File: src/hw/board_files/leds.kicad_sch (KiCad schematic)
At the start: 19 parts, among them U1 IS31FL3236A-TQ

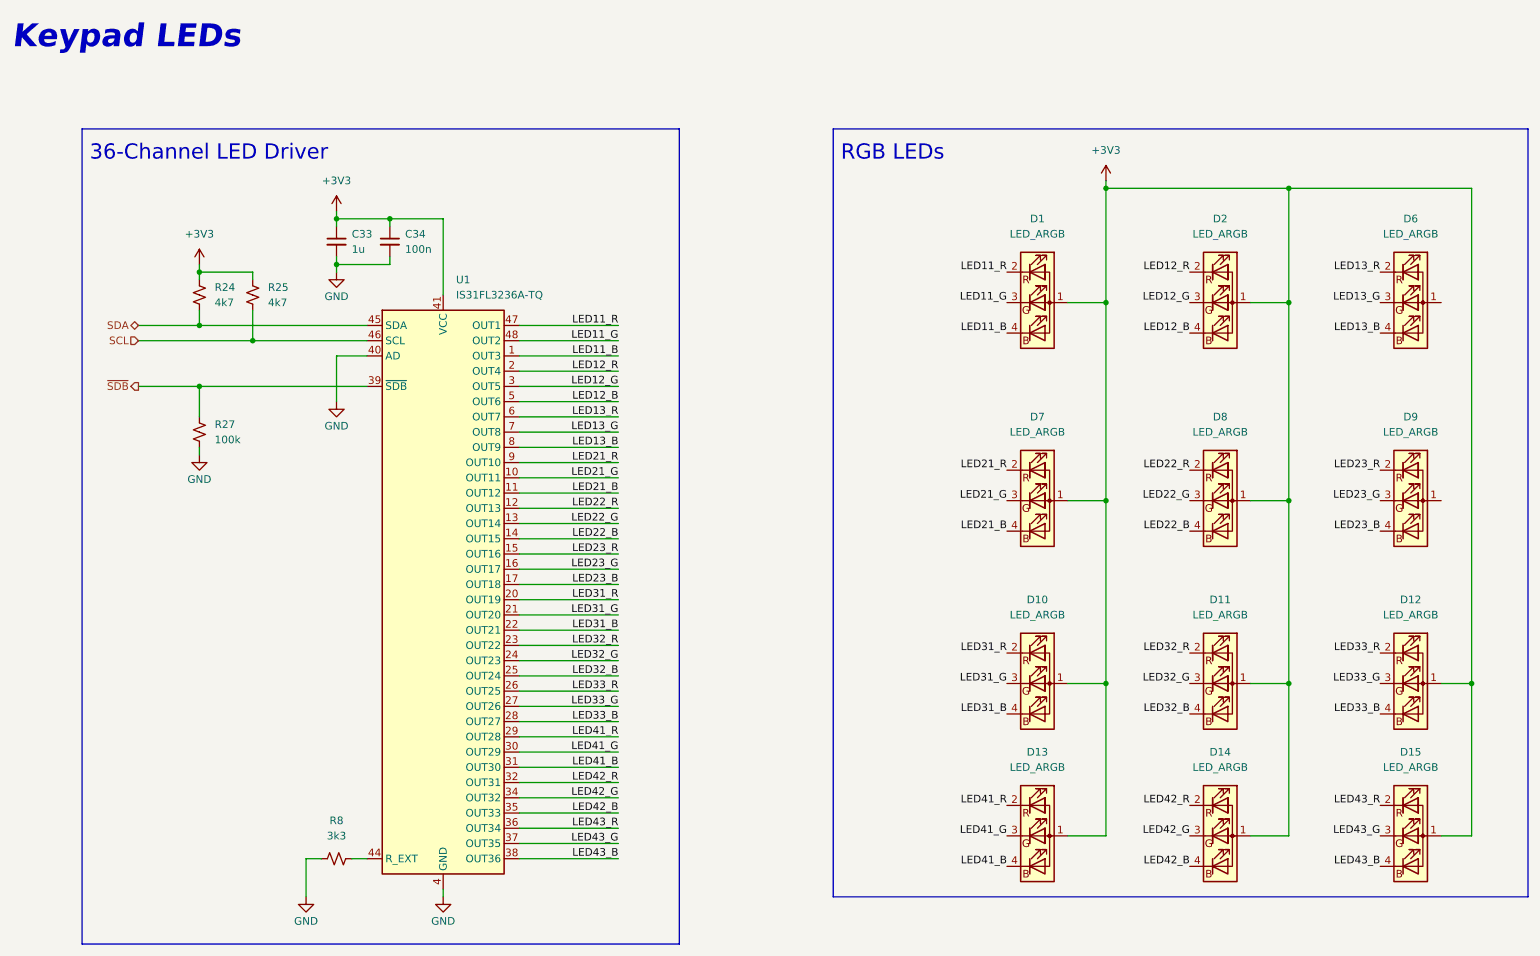
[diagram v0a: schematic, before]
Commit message: Added all footprints, need to connect switches to MCU
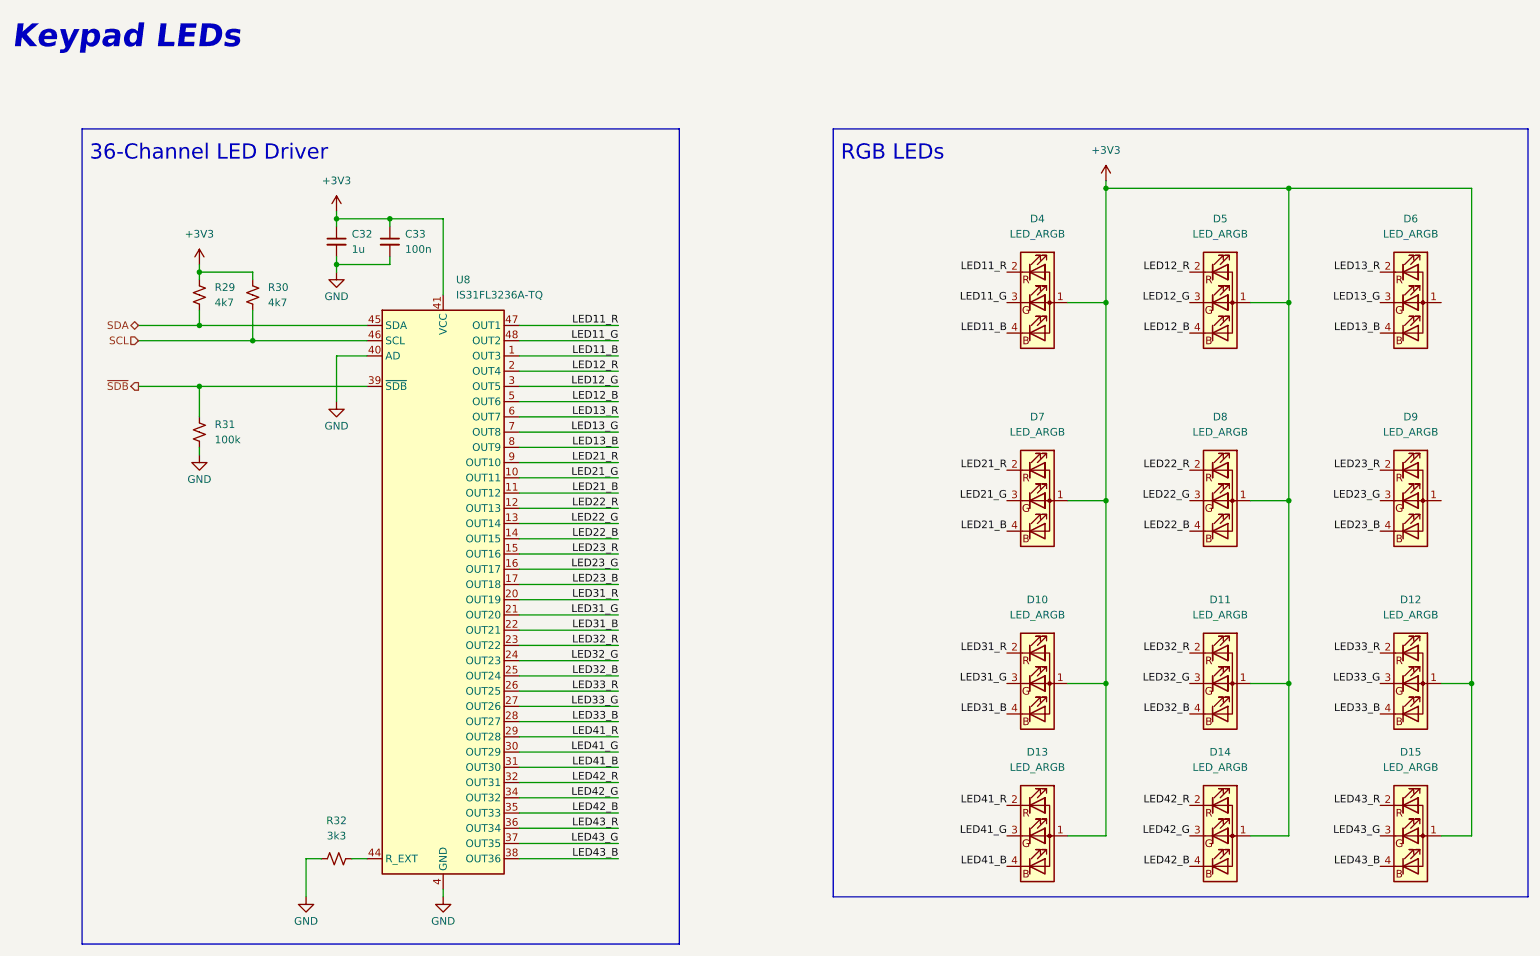
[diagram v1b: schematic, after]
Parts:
- C32: renamed from C33; footprint (none) -> Capacitor_SMD:C_0603_1608Metric_Pad1.08x0.95mm_HandSolder
- C33: renamed from C34; footprint (none) -> Capacitor_SMD:C_0603_1608Metric_Pad1.08x0.95mm_HandSolder
- D10, D11, D12, D13, D14, D15, D6, D7, D8, D9: footprint (none) -> Project_Library:RGB_LED_6028_Reverse_Mount
- D4: renamed from D1; footprint (none) -> Project_Library:RGB_LED_6028_Reverse_Mount
- D5: renamed from D2; footprint (none) -> Project_Library:RGB_LED_6028_Reverse_Mount
- R29: renamed from R24; footprint (none) -> Resistor_SMD:R_0805_2012Metric_Pad1.20x1.40mm_HandSolder
- R30: renamed from R25; footprint (none) -> Resistor_SMD:R_0805_2012Metric_Pad1.20x1.40mm_HandSolder
- R31: renamed from R27; footprint (none) -> Resistor_SMD:R_0603_1608Metric_Pad0.98x0.95mm_HandSolder
- R32: renamed from R8; footprint (none) -> Resistor_SMD:R_0805_2012Metric_Pad1.20x1.40mm_HandSolder
- renumbered U1 to U8
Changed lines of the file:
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@@
 		(dnp no)
 		(fields_autoplaced yes)
-		(property "Reference" "#PWR025"
+		(property "Reference" "#PWR071"
 			(at 195.58 44.45 0)
 			(effects
@@
 			(project "keypad_usb_hub"
 				(path "/62136966-d911-451f-9518-a7827b282fe3/2edcea5b-cb36-4170-89ba-0ae1b39f10ac"
-					(reference "#PWR025")
+					(reference "#PWR071")
 					(unit 1)
 				)
@@
 		(on_board yes)
 		(dnp no)
-		(property "Reference" "#PWR060"
+		(property "Reference" "#PWR076"
 			(at 44.45 92.71 0)
 			(effects
@@
 			(project "keypad_usb_hub"
 				(path "/62136966-d911-451f-9518-a7827b282fe3/2edcea5b-cb36-4170-89ba-0ae1b39f10ac"
-					(reference "#PWR060")
+					(reference "#PWR076")
 					(unit 1)
 				)
@@
 		(dnp no)
 		(fields_autoplaced yes)
-		(property "Reference" "C33"
+		(property "Reference" "C32"
 			(at 69.85 49.5362 0)
 			(effects
@@
 			)
 		)
-		(property "Footprint" ""
+		(property "Footprint" "Capacitor_SMD:C_0603_1608Metric_Pad1.08x0.95mm_HandSolder"
 			(at 67.31 50.8 0)
 			(effects
@@
 			(project "keypad_usb_hub"
 				(path "/62136966-d911-451f-9518-a7827b282fe3/2edcea5b-cb36-4170-89ba-0ae1b39f10ac"
-					(reference "C33")
+					(reference "C32")
 					(unit 1)
 				)
@@
 			)
 		)
-		(property "Footprint" ""
+		(property "Footprint" "Project_Library:RGB_LED_6028_Reverse_Mount"
 			(at 246.38 151.13 0)
 			(effects
@@
 			)
 		)
-		(property "Footprint" ""
+		(property "Footprint" "Project_Library:RGB_LED_6028_Reverse_Mount"
 			(at 184.15 125.73 0)
 			(effects
@@
 			)
 		)
-		(property "Footprint" ""
+		(property "Footprint" "Project_Library:RGB_LED_6028_Reverse_Mount"
 			(at 184.15 151.13 0)
 			(effects
@@
 			)
 		)
-		(property "Footprint" ""
+		(property "Footprint" "Project_Library:RGB_LED_6028_Reverse_Mount"
 			(at 214.63 151.13 0)
 			(effects
@@
 			)
 		)
-		(property "Footprint" ""
+		(property "Footprint" "Project_Library:RGB_LED_6028_Reverse_Mount"
 			(at 214.63 125.73 0)
 			(effects
@@
 		(dnp no)
 		(fields_autoplaced yes)
-		(property "Reference" "U1"
+		(property "Reference" "U8"
 			(at 87.2333 57.15 0)
 			(effects
@@
 			(project "keypad_usb_hub"
 				(path "/62136966-d911-451f-9518-a7827b282fe3/2edcea5b-cb36-4170-89ba-0ae1b39f10ac"
-					(reference "U1")
+					(reference "U8")
 					(unit 1)
 				)
@@
 			)
 		)
-		(property "Footprint" ""
+		(property "Footprint" "Project_Library:RGB_LED_6028_Reverse_Mount"
 			(at 184.15 95.25 0)
 			(effects
@@
 		(dnp no)
 		(fields_autoplaced yes)
-		(property "Reference" "D1"
+		(property "Reference" "D4"
 			(at 184.15 46.99 0)
 			(effects
@@
 			)
 		)
-		(property "Footprint" ""
+		(property "Footprint" "Project_Library:RGB_LED_6028_Reverse_Mount"
 			(at 184.15 62.23 0)
 			(effects
@@
 			(project "keypad_usb_hub"
 				(path "/62136966-d911-451f-9518-a7827b282fe3/2edcea5b-cb36-4170-89ba-0ae1b39f10ac"
-					(reference "D1")
+					(reference "D4")
 					(unit 1)
 				)
@@
 		(dnp no)
 		(fields_autoplaced yes)
-		(property "Reference" "R24"
+		(property "Reference" "R29"
 			(at 46.99 58.4199 0)
 			(effects
@@
 			)
 		)
-		(property "Footprint" ""
+		(property "Footprint" "Resistor_SMD:R_0805_2012Metric_Pad1.20x1.40mm_HandSolder"
 			(at 44.45 59.69 0)
 			(effects
@@
 			(project "keypad_usb_hub"
 				(path "/62136966-d911-451f-9518-a7827b282fe3/2edcea5b-cb36-4170-89ba-0ae1b39f10ac"
-					(reference "R24")
+					(reference "R29")
 					(unit 1)
 				)
@@
 			)
 		)
-		(property "Footprint" ""
+		(property "Footprint" "Project_Library:RGB_LED_6028_Reverse_Mount"
 			(at 214.63 95.25 0)
 			(effects
@@
 		(dnp no)
 		(fields_autoplaced yes)
-		(property "Reference" "#PWR061"
+		(property "Reference" "#PWR073"
 			(at 44.45 58.42 0)
 			(effects
@@
 			(project "keypad_usb_hub"
 				(path "/62136966-d911-451f-9518-a7827b282fe3/2edcea5b-cb36-4170-89ba-0ae1b39f10ac"
-					(reference "#PWR061")
+					(reference "#PWR073")
 					(unit 1)
 				)
@@
 		(dnp no)
 		(fields_autoplaced yes)
-		(property "Reference" "R8"
+		(property "Reference" "R32"
 			(at 67.31 147.32 90)
 			(effects
@@
 			)
 		)
-		(property "Footprint" ""
+		(property "Footprint" "Resistor_SMD:R_0805_2012Metric_Pad1.20x1.40mm_HandSolder"
 			(at 67.31 153.67 0)
 			(effects
@@
 			(project "keypad_usb_hub"
 				(path "/62136966-d911-451f-9518-a7827b282fe3/2edcea5b-cb36-4170-89ba-0ae1b39f10ac"
-					(reference "R8")
+					(reference "R32")
 					(unit 1)
 				)
@@
 		(dnp no)
 		(fields_autoplaced yes)
-		(property "Reference" "R27"
+		(property "Reference" "R31"
 			(at 46.99 81.2799 0)
 			(effects
@@
 			)
 		)
-		(property "Footprint" ""
+		(property "Footprint" "Resistor_SMD:R_0603_1608Metric_Pad0.98x0.95mm_HandSolder"
 			(at 44.45 82.55 0)
 			(effects
@@
 			(project "keypad_usb_hub"
 				(path "/62136966-d911-451f-9518-a7827b282fe3/2edcea5b-cb36-4170-89ba-0ae1b39f10ac"
-					(reference "R27")
+					(reference "R31")
 					(unit 1)
 				)
@@
 		(dnp no)
 		(fields_autoplaced yes)
-		(property "Reference" "#PWR056"
+		(property "Reference" "#PWR072"
 			(at 67.31 49.53 0)
 			(effects
@@
 			(project "keypad_usb_hub"
 				(path "/62136966-d911-451f-9518-a7827b282fe3/2edcea5b-cb36-4170-89ba-0ae1b39f10ac"
-					(reference "#PWR056")
+					(reference "#PWR072")
 					(unit 1)
 				)
@@
 		(on_board yes)
 		(dnp no)
-		(property "Reference" "#PWR057"
+		(property "Reference" "#PWR074"
 			(at 67.31 62.23 0)
 			(effects
@@
 			(project "keypad_usb_hub"
 				(path "/62136966-d911-451f-9518-a7827b282fe3/2edcea5b-cb36-4170-89ba-0ae1b39f10ac"
-					(reference "#PWR057")
+					(reference "#PWR074")
 					(unit 1)
 				)
@@
 		(on_board yes)
 		(dnp no)
-		(property "Reference" "#PWR024"
+		(property "Reference" "#PWR077"
 			(at 62.23 166.37 0)
 			(effects
@@
 			(project "keypad_usb_hub"
 				(path "/62136966-d911-451f-9518-a7827b282fe3/2edcea5b-cb36-4170-89ba-0ae1b39f10ac"
-					(reference "#PWR024")
+					(reference "#PWR077")
 					(unit 1)
 				)
@@
 		(dnp no)
 		(fields_autoplaced yes)
-		(property "Reference" "C34"
+		(property "Reference" "C33"
 			(at 78.74 49.5362 0)
 			(effects
@@
 			)
 		)
-		(property "Footprint" ""
+		(property "Footprint" "Capacitor_SMD:C_0603_1608Metric_Pad1.08x0.95mm_HandSolder"
 			(at 76.2 50.8 0)
 			(effects
@@
 			(project "keypad_usb_hub"
 				(path "/62136966-d911-451f-9518-a7827b282fe3/2edcea5b-cb36-4170-89ba-0ae1b39f10ac"
-					(reference "C34")
+					(reference "C33")
 					(unit 1)
 				)
@@
 			)
 		)
-		(property "Footprint" ""
+		(property "Footprint" "Project_Library:RGB_LED_6028_Reverse_Mount"
 			(at 246.38 95.25 0)
 			(effects
@@
 			)
 		)
-		(property "Footprint" ""
+		(property "Footprint" "Project_Library:RGB_LED_6028_Reverse_Mount"
 			(at 246.38 62.23 0)
 			(effects
@@
 		(on_board yes)
 		(dnp no)
-		(property "Reference" "#PWR023"
+		(property "Reference" "#PWR078"
 			(at 85.09 166.37 0)
 			(effects
@@
 			(project "keypad_usb_hub"
 				(path "/62136966-d911-451f-9518-a7827b282fe3/2edcea5b-cb36-4170-89ba-0ae1b39f10ac"
-					(reference "#PWR023")
+					(reference "#PWR078")
 					(unit 1)
 				)
@@
 		(dnp no)
 		(fields_autoplaced yes)
-		(property "Reference" "D2"
+		(property "Reference" "D5"
 			(at 214.63 46.99 0)
 			(effects
@@
 			)
 		)
-		(property "Footprint" ""
+		(property "Footprint" "Project_Library:RGB_LED_6028_Reverse_Mount"
 			(at 214.63 62.23 0)
 			(effects
@@
 			(project "keypad_usb_hub"
 				(path "/62136966-d911-451f-9518-a7827b282fe3/2edcea5b-cb36-4170-89ba-0ae1b39f10ac"
-					(reference "D2")
+					(reference "D5")
 					(unit 1)
 				)
@@
 		(on_board yes)
 		(dnp no)
-		(property "Reference" "#PWR058"
+		(property "Reference" "#PWR075"
 			(at 67.31 83.82 0)
 			(effects
@@
 			(project "keypad_usb_hub"
 				(path "/62136966-d911-451f-9518-a7827b282fe3/2edcea5b-cb36-4170-89ba-0ae1b39f10ac"
-					(reference "#PWR058")
+					(reference "#PWR075")
 					(unit 1)
 				)
@@
 			)
 		)
-		(property "Footprint" ""
+		(property "Footprint" "Project_Library:RGB_LED_6028_Reverse_Mount"
 			(at 246.38 125.73 0)
 			(effects
@@
 		(dnp no)
 		(fields_autoplaced yes)
-		(property "Reference" "R25"
+		(property "Reference" "R30"
 			(at 55.88 58.4199 0)
 			(effects
@@
 			)
 		)
-		(property "Footprint" ""
+		(property "Footprint" "Resistor_SMD:R_0805_2012Metric_Pad1.20x1.40mm_HandSolder"
 			(at 53.34 59.69 0)
 			(effects
@@
 			(project "keypad_usb_hub"
 				(path "/62136966-d911-451f-9518-a7827b282fe3/2edcea5b-cb36-4170-89ba-0ae1b39f10ac"
-					(reference "R25")
-					(unit 1)
-				)
+					(reference "R30")
+					(unit 1)
+				)

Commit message: Added rotary encoder and OLED. Started laying out board then I need to review schematic and change pinout if needed
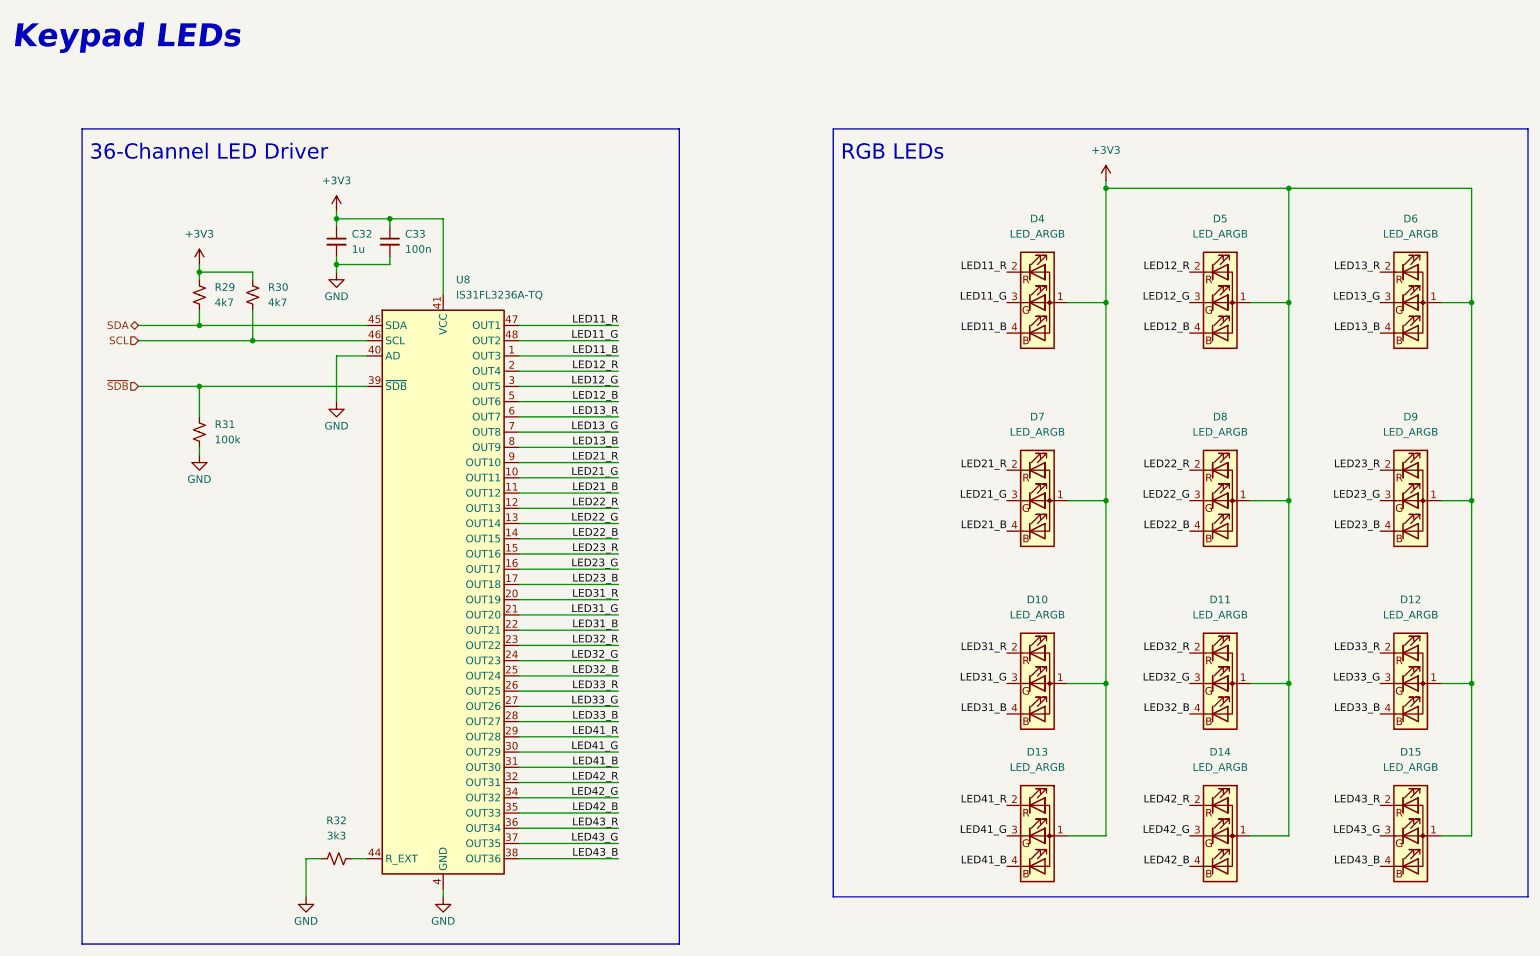
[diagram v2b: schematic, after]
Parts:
- R29, R30, R32: footprint Resistor_SMD:R_0805_2012Metric_Pad1.20x1.40mm_HandSolder -> Resistor_SMD:R_0603_1608Metric_Pad0.98x0.95mm_HandSolder
- R31: footprint Resistor_SMD:R_0603_1608Metric_Pad0.98x0.95mm_HandSolder -> Resistor_SMD:R_0805_2012Metric_Pad1.20x1.40mm_HandSolder
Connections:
- net +3V3: now also D6.1 (A), D9.1 (A)
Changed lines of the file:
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@@
 	)
 	(junction
+		(at 256.54 60.96)
+		(diameter 0)
+		(color 0 0 0 0)
+	)
+	(junction
 		(at 226.06 41.91)
 		(diameter 0)
@@
 	)
 	(junction
+		(at 256.54 93.98)
+		(diameter 0)
+		(color 0 0 0 0)
+	)
+	(junction
 		(at 53.34 67.31)
 		(diameter 0)
@@
 	(wire
 		(pts
-			(xy 256.54 41.91) (xy 256.54 124.46)
+			(xy 256.54 41.91) (xy 256.54 60.96)
 		)
 		(stroke
@@
 	(wire
 		(pts
+			(xy 256.54 93.98) (xy 256.54 124.46)
+		)
+		(stroke
+			(width 0)
+			(type default)
+		)
+	)
+	(wire
+		(pts
 			(xy 97.79 146.05) (xy 114.3 146.05)
 		)
@@
 	(wire
 		(pts
+			(xy 251.46 60.96) (xy 256.54 60.96)
+		)
+		(stroke
+			(width 0)
+			(type default)
+		)
+	)
+	(wire
+		(pts
 			(xy 97.79 100.33) (xy 114.3 100.33)
 		)
@@
 	(wire
 		(pts
+			(xy 251.46 93.98) (xy 256.54 93.98)
+		)
+		(stroke
+			(width 0)
+			(type default)
+		)
+	)
+	(wire
+		(pts
 			(xy 195.58 60.96) (xy 195.58 41.91)
 		)
@@
 	(wire
 		(pts
+			(xy 256.54 60.96) (xy 256.54 93.98)
+		)
+		(stroke
+			(width 0)
+			(type default)
+		)
+	)
+	(wire
+		(pts
 			(xy 195.58 149.86) (xy 195.58 124.46)
 		)
@@
 	)
 	(hierarchical_label "~{SDB}"
-		(shape output)
+		(shape input)
 		(at 34.29 74.93 180)
 		(effects
@@
 			)
 		)
-		(property "Footprint" "Resistor_SMD:R_0805_2012Metric_Pad1.20x1.40mm_HandSolder"
+		(property "Footprint" "Resistor_SMD:R_0603_1608Metric_Pad0.98x0.95mm_HandSolder"
 			(at 44.45 59.69 0)
 			(effects
@@
 			)
 		)
-		(property "Footprint" "Resistor_SMD:R_0805_2012Metric_Pad1.20x1.40mm_HandSolder"
+		(property "Footprint" "Resistor_SMD:R_0603_1608Metric_Pad0.98x0.95mm_HandSolder"
 			(at 67.31 153.67 0)
 			(effects
@@
 			)
 		)
-		(property "Footprint" "Resistor_SMD:R_0603_1608Metric_Pad0.98x0.95mm_HandSolder"
+		(property "Footprint" "Resistor_SMD:R_0805_2012Metric_Pad1.20x1.40mm_HandSolder"
 			(at 44.45 82.55 0)
 			(effects
@@
 			)
 		)
-		(property "Footprint" "Resistor_SMD:R_0805_2012Metric_Pad1.20x1.40mm_HandSolder"
+		(property "Footprint" "Resistor_SMD:R_0603_1608Metric_Pad0.98x0.95mm_HandSolder"
 			(at 53.34 59.69 0)
 			(effects
